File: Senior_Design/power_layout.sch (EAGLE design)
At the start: 105 parts, among them J1 AU-Y1008-2, J1[SIMCARD] 78646-3001, J2 U.FL-R-SMT-1(01), J3 U.FL-R-SMT-1(01), J4[GROVE] 640456-4, T1 BCX70SMD, T2 BCX70SMD, U1 SIM7000E, U2 TUSB2046BVFR, U3 MAX3373EEKA+T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

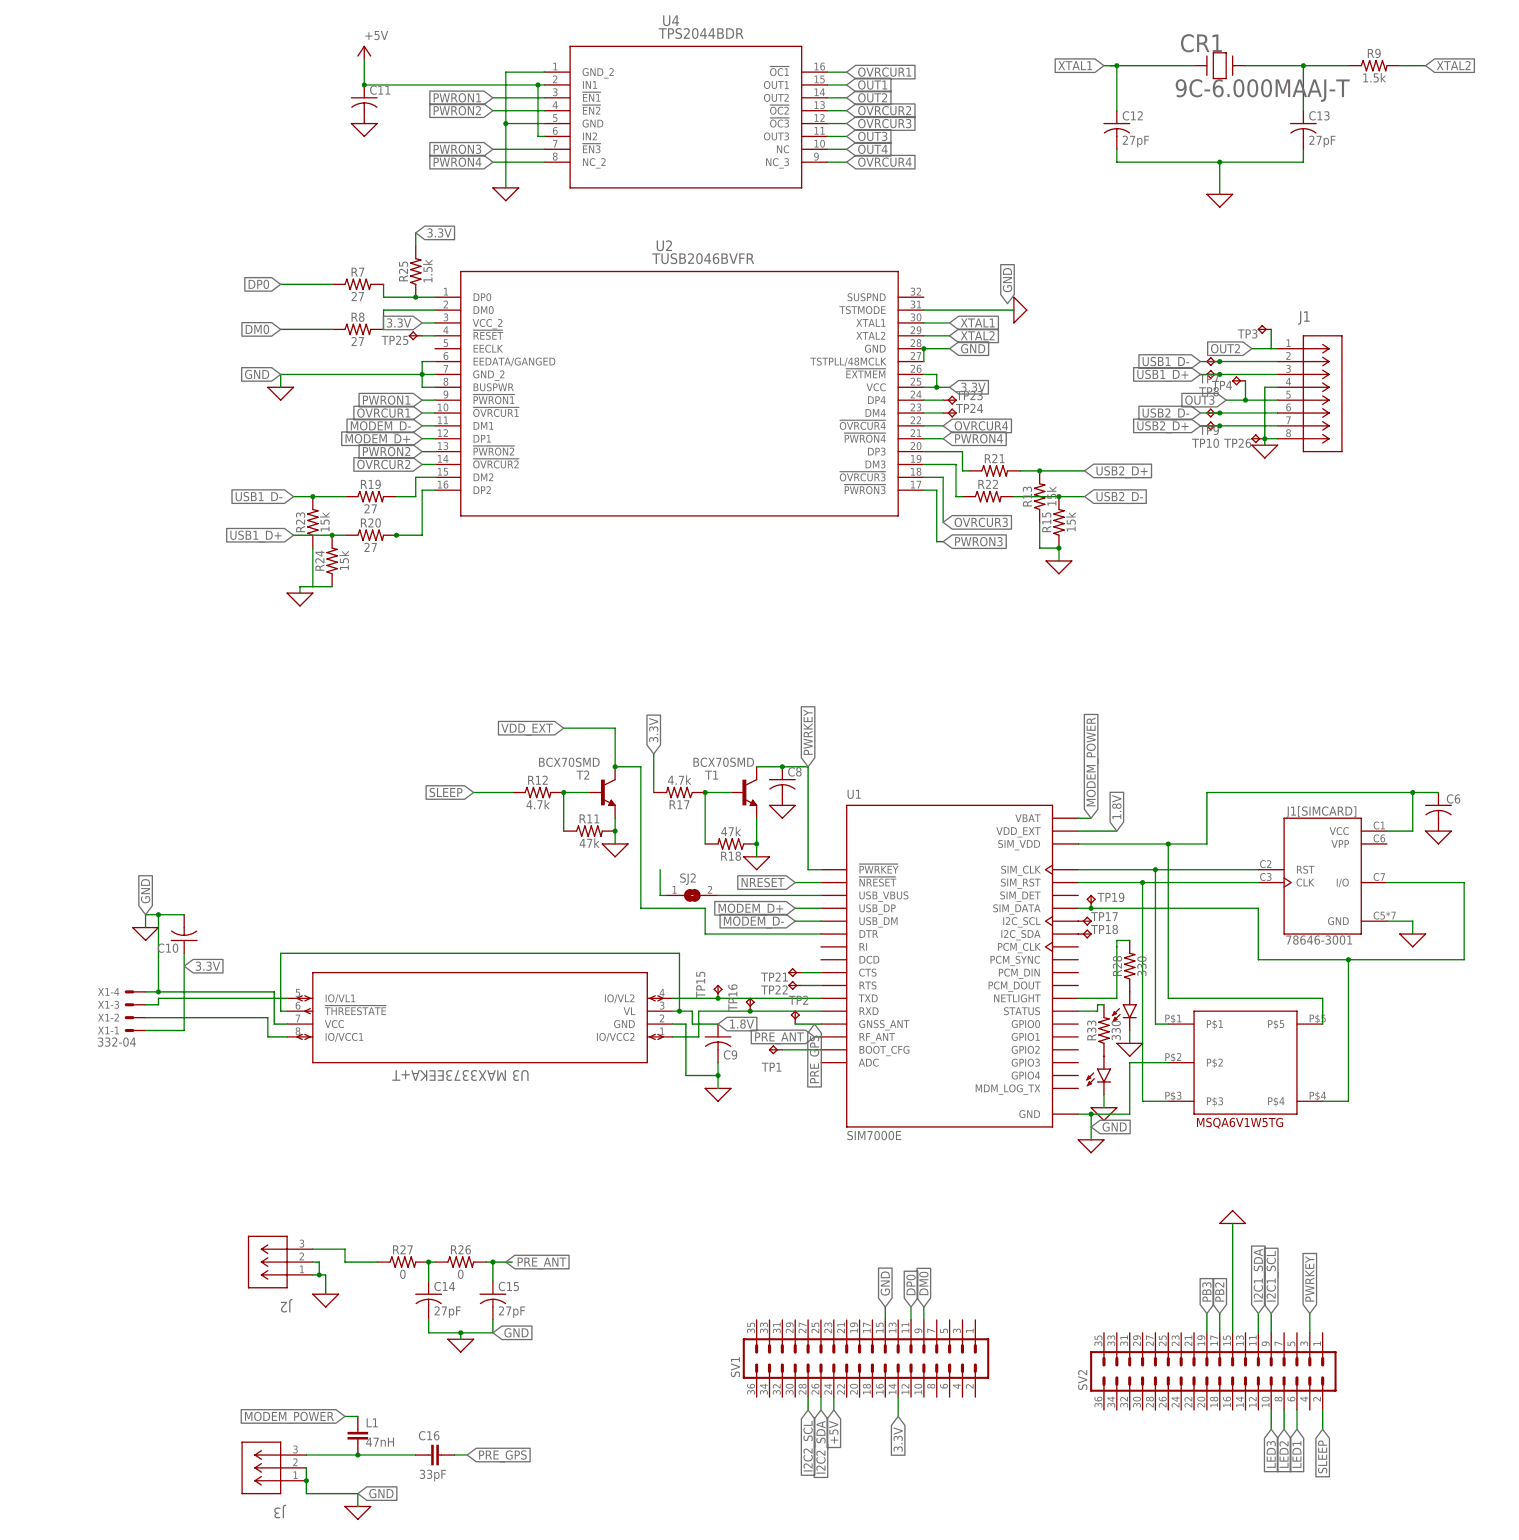
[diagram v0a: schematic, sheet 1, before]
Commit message: Updating missing part values
Alex had assigned these before but I wrote over them on accident :)
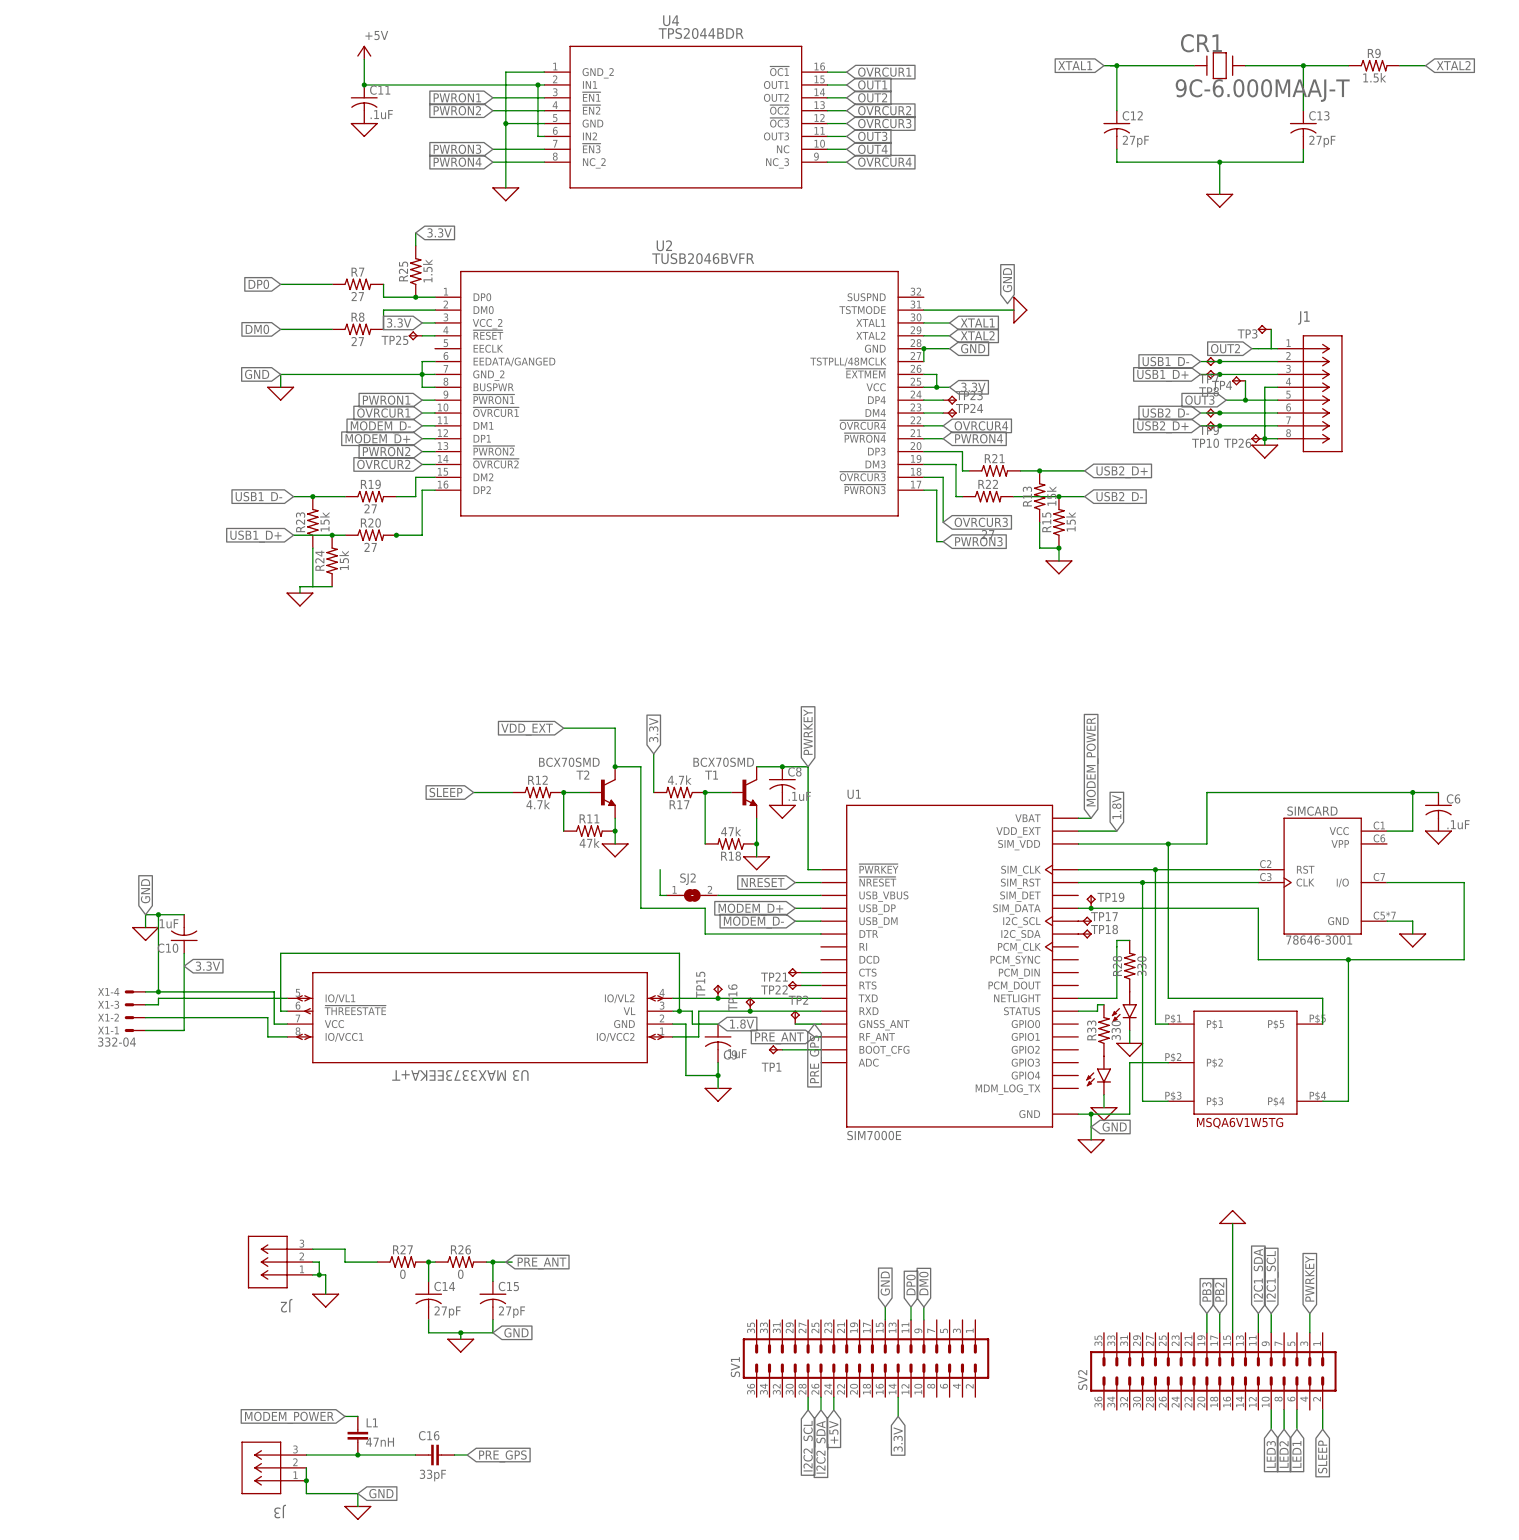
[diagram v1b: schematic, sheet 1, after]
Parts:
- C1: value (none) -> 100uF
- C10, C11, C6, C8, C9: value (none) -> .1uF
- C4: value (none) -> 1uF
- R10, R14, R16: value (none) -> 4700
- R21, R22: value (none) -> 27
- R4: value (none) -> 47k
- R5: value (none) -> 100k
- R6: value (none) -> 470k
- renumbered J1[SIMCARD] to SIMCARD, J4[GROVE] to GROVE2, U$1 to U5

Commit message: Beta Boar Spin Files
Implemented board revisions from Alpha board.
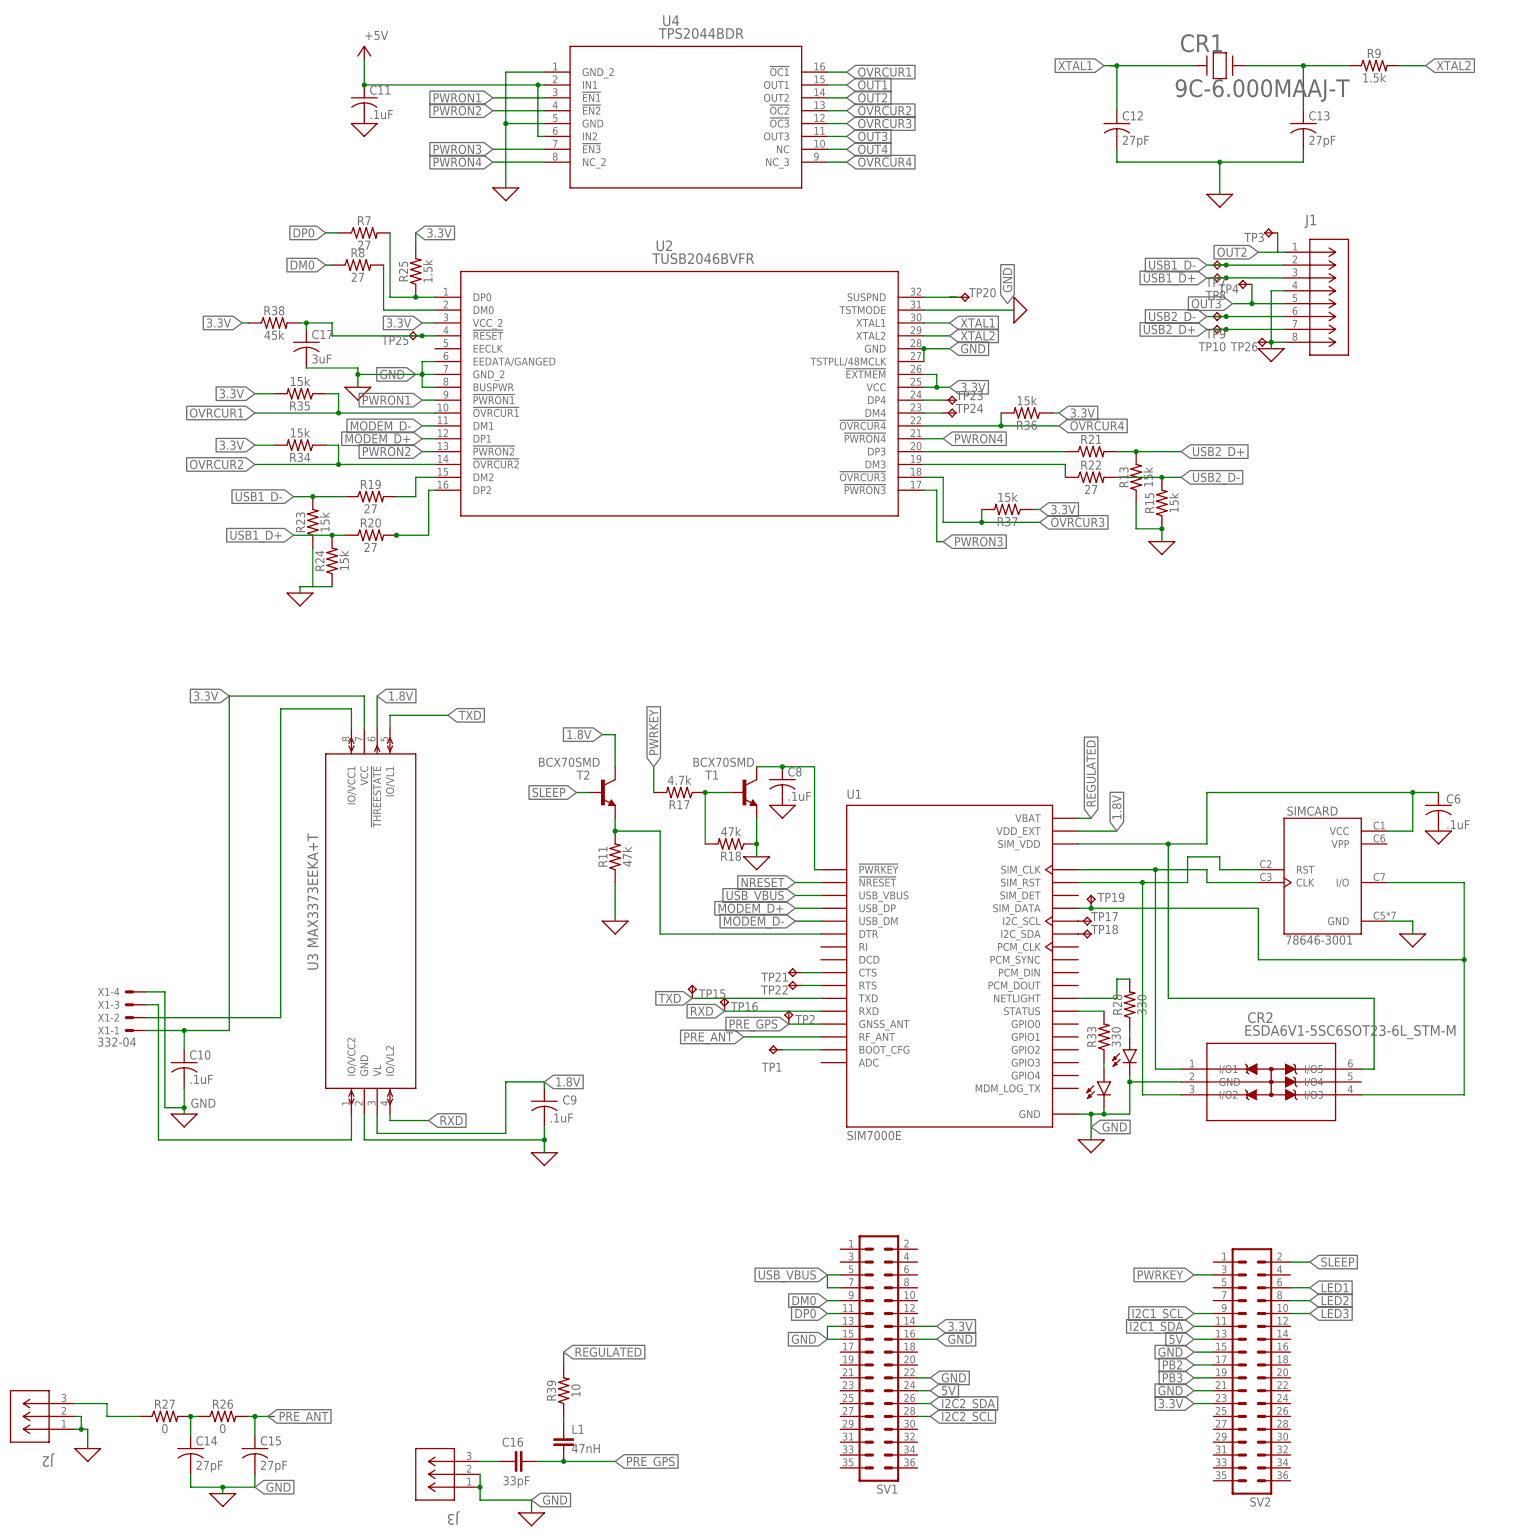
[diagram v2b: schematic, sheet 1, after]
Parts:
- removed R12: 4.7k, SparkFun-Resistors:4.7KOHM-0603-1/10W-1%
- removed SJ1: (no value), jumper:SJ2W
- removed SJ2: (no value), jumper:SJ
- removed SW1, SW2, SW3: (no value), adafruit:SWITCH_PUSHBUTTONSOFTTOUCHSMD_SJ
- removed U5: MSQA6V1W5T2G, Personal:MSQA6V1W5T2G
- added BTN2, BTN3, RESET: PTS636SM25F, Personal:PTS636SM25F
- added C17: 3uF, rcl:C-USC0805
- added CR2: ESDA6V1-5SC6SOT23-6L_STM-M, Personal:ESDA6V1-5SC6SOT23-6L_STM-M
- added R34, R35, R36, R37: 15k, SparkFun-Resistors:RESISTOR0805
- added R38: 45k, SparkFun-Resistors:RESISTOR0805
- added R39: 10, SparkFun-Resistors:RESISTOR0805
- added TP20: TPTP10R, testpad:TPTP10R
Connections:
- removed net +5V: C1.1, C11.1, C4.1, POWER_SUPPLY.EN, POWER_SUPPLY.VIN, SJ2.1, SV1.24, TP6.TP, U4.IN1, U4.IN2
- removed net MODEM_POWER: C3.1, C5.1, L1.1, SJ1.2, TP5.TP, U1.VBAT
- removed net N$16 (its old number): U3.IO/VL1, X1-3.S
- removed net N$17: R11.1, R12.2, T2.B
- removed net VDD_EXT: T2.C, U1.DTR
- new net 0: R11.1
- new net 5V: C1.1, C11.1, C4.1, POWER_SUPPLY.EN, POWER_SUPPLY.VIN, SV1.24, SV2.13, TP6.TP, U4.IN1, U4.IN2
- new net N$23: C8.1, T1.C, U1.!PWRKEY
- new net N$38: U3.IO/VCC2, X1-3.S
- new net RXD: TP16.TP, U1.RXD, U3.IO/VL2
- new net TXD: TP15.TP, U1.TXD, U3.IO/VL1
- new net USB_VBUS: SV1.5, SV1.7, U1.USB_VBUS
- net 1.8V: now also T2.C
- net 3.3V: now also BTN2.1, BTN3.1, R34.2, R35.2, R36.1, R37.1, R38.1, RESET.1, SV2.23, U3.VCC; no longer R17.2, SJ1.1, SW1.P$2, SW2.P$2, SW3.P$2
- net GND: now also C17.2, CR2.GND, SV1.13, SV1.16, SV1.22, SV2.21; no longer R11.2, T2.E, U3.VCC, U5.P$2
- net N$1: now also CR2.I/O5; no longer U5.P$5
- net N$15: no longer L1.2
- net N$2: now also CR2.I/O2, SIMCARD.RST; no longer SIMCARD.CLK, U5.P$3
- net N$27: now also L1.1, R39.1; no longer TP16.TP, U1.RXD, U3.IO/VCC2
- net N$28: now also TP20.TP, U2.SUSPND; no longer TP15.TP, U1.TXD, U3.IO/VL2
- net N$34: now also C17.1, R38.2
- net N$36: now also R11.2, T2.E, U1.DTR; no longer SJ2.2, U1.USB_VBUS
- net N$4: now also CR2.I/O1, SIMCARD.CLK; no longer SIMCARD.RST, U5.P$1
- net N$6: now also CR2.I/O3; no longer U5.P$4
- net NRESET: now also RESET.2; no longer SW1.P$1
- net OVRCUR1: now also R35.1
- net OVRCUR2: now also R34.1
- net OVRCUR3: now also R37.2
- net OVRCUR4: now also R36.2
- net PB2: now also BTN2.2; no longer SW2.P$1
- net PB3: now also BTN3.2; no longer SW3.P$1
- net PRE_GPS: now also L1.2
- net PWRKEY: now also R17.2; no longer C8.1, T1.C, U1.!PWRKEY
- net REGULATED: now also C3.1, C5.1, R39.2, TP5.TP, U1.VBAT; no longer SJ1.3
- net SLEEP: now also T2.B; no longer R12.1
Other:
- moved on the sheet: C10, C14, C15, C16, C9, J1, J2, J3, L1, R11, R13, R15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
